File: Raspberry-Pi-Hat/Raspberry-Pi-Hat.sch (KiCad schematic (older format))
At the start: 60 parts, among them J1 Screw_Terminal_01x04, J2 Screw_Terminal_01x02, J3 40HAT, J4 Screw_Terminal_01x02, J5 USB_B, J6 CONN_02X02, J7 USB_A, J8 USB_A, J9 CONN_01X02, Q1 DMG2305UX, Q2 DMMT5401, U1 ADM3490ExR, U2 CAT24C32, U3 TCAN330, U4 LMZ13608

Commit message: changed footprint size
changed resistor and capacitor footprint size for 0603 when possible.
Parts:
- C10, C11, C12, C13, C16, C17, C18, C2, C3, C4, C5, C50, C51, C6, C7, C8, C9: footprint Capacitor_SMD:C_1206_3216Metric_Pad1.42x1.75mm_HandSolder -> Capacitor_SMD:C_0603_1608Metric_Pad1.05x0.95mm_HandSolder
- R1, R10, R2, R3, R4, R5: footprint Resistor_SMD:R_1206_3216Metric_Pad1.42x1.75mm_HandSolder -> Resistor_SMD:R_0603_1608Metric_Pad1.05x0.95mm_HandSolder
- R11, R23, R24, R6, R7, R8, R9: footprint Resistor_SMD:R_0603_1608Metric_Pad0.84x1.00mm_HandSolder -> Resistor_SMD:R_0603_1608Metric_Pad1.05x0.95mm_HandSolder
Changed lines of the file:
@@
 F 0 "R23" V 5830 3600 50  0000 C CNN
 F 1 "10K" V 5750 3600 50  0000 C CNN
-F 2 "Resistor_SMD:R_0603_1608Metric_Pad0.84x1.00mm_HandSolder" V 5680 3600 50  0001 C CNN
+F 2 "Resistor_SMD:R_0603_1608Metric_Pad1.05x0.95mm_HandSolder" V 5680 3600 50  0001 C CNN
 F 3 "" H 5750 3600 50  0001 C CNN
 	1    5750 3600
@@
 F 0 "R24" V 6630 3600 50  0000 C CNN
 F 1 "47K" V 6550 3600 50  0000 C CNN
-F 2 "Resistor_SMD:R_0603_1608Metric_Pad0.84x1.00mm_HandSolder" V 6480 3600 50  0001 C CNN
+F 2 "Resistor_SMD:R_0603_1608Metric_Pad1.05x0.95mm_HandSolder" V 6480 3600 50  0001 C CNN
 F 3 "" H 6550 3600 50  0001 C CNN
 	1    6550 3600
@@
 F 0 "R6" V 2430 7400 50  0000 C CNN
 F 1 "3.9K" V 2350 7400 50  0000 C CNN
-F 2 "Resistor_SMD:R_0603_1608Metric_Pad0.84x1.00mm_HandSolder" V 2280 7400 50  0001 C CNN
+F 2 "Resistor_SMD:R_0603_1608Metric_Pad1.05x0.95mm_HandSolder" V 2280 7400 50  0001 C CNN
 F 3 "" H 2350 7400 50  0001 C CNN
 	1    2350 7400
@@
 F 0 "R8" V 2430 7650 50  0000 C CNN
 F 1 "3.9K" V 2350 7650 50  0000 C CNN
-F 2 "Resistor_SMD:R_0603_1608Metric_Pad0.84x1.00mm_HandSolder" V 2280 7650 50  0001 C CNN
+F 2 "Resistor_SMD:R_0603_1608Metric_Pad1.05x0.95mm_HandSolder" V 2280 7650 50  0001 C CNN
 F 3 "" H 2350 7650 50  0001 C CNN
 	1    2350 7650
@@
 F 0 "R7" V 6180 4300 50  0000 C CNN
 F 1 "DNP" V 6100 4300 50  0000 C CNN
-F 2 "Resistor_SMD:R_0603_1608Metric_Pad0.84x1.00mm_HandSolder" V 6030 4300 50  0001 C CNN
+F 2 "Resistor_SMD:R_0603_1608Metric_Pad1.05x0.95mm_HandSolder" V 6030 4300 50  0001 C CNN
 F 3 "" H 6100 4300 50  0001 C CNN
 	1    6100 4300
@@
 F 0 "R9" V 6180 4950 50  0000 C CNN
 F 1 "DNP" V 6100 4950 50  0000 C CNN
-F 2 "Resistor_SMD:R_0603_1608Metric_Pad0.84x1.00mm_HandSolder" V 6030 4950 50  0001 C CNN
+F 2 "Resistor_SMD:R_0603_1608Metric_Pad1.05x0.95mm_HandSolder" V 6030 4950 50  0001 C CNN
 F 3 "" H 6100 4950 50  0001 C CNN
 	1    6100 4950
@@
 F 0 "R11" V 1380 6100 50  0000 C CNN
 F 1 "DNP" V 1300 6100 50  0000 C CNN
-F 2 "Resistor_SMD:R_0603_1608Metric_Pad0.84x1.00mm_HandSolder" V 1230 6100 50  0001 C CNN
+F 2 "Resistor_SMD:R_0603_1608Metric_Pad1.05x0.95mm_HandSolder" V 1230 6100 50  0001 C CNN
 F 3 "" H 1300 6100 50  0001 C CNN
 	1    1300 6100
@@
 F 0 "C10" H 12215 2046 50  0000 L CNN
 F 1 "470nF" H 12215 1955 50  0000 L CNN
-F 2 "Capacitor_SMD:C_1206_3216Metric_Pad1.42x1.75mm_HandSolder" H 12138 1850 50  0001 C CNN
+F 2 "Capacitor_SMD:C_0603_1608Metric_Pad1.05x0.95mm_HandSolder" H 12138 1850 50  0001 C CNN
 F 3 "~" H 12100 2000 50  0001 C CNN
 	1    12100 2000
@@
 F 0 "C16" H 15065 1796 50  0000 L CNN
 F 1 "47uF" H 15065 1705 50  0000 L CNN
-F 2 "Capacitor_SMD:C_1206_3216Metric_Pad1.42x1.75mm_HandSolder" H 14988 1600 50  0001 C CNN
+F 2 "Capacitor_SMD:C_0603_1608Metric_Pad1.05x0.95mm_HandSolder" H 14988 1600 50  0001 C CNN
 F 3 "~" H 14950 1750 50  0001 C CNN
 F 4 "X5R ceramic" H 14950 1750 50  0001 C CNN "Technologie"
@@
 F 0 "C17" H 15515 1796 50  0000 L CNN
 F 1 "47nF" H 15515 1705 50  0000 L CNN
-F 2 "Capacitor_SMD:C_1206_3216Metric_Pad1.42x1.75mm_HandSolder" H 15438 1600 50  0001 C CNN
+F 2 "Capacitor_SMD:C_0603_1608Metric_Pad1.05x0.95mm_HandSolder" H 15438 1600 50  0001 C CNN
 F 3 "~" H 15400 1750 50  0001 C CNN
 F 4 "X5R ceramic" H 15400 1750 50  0001 C CNN "Technologie"
@@
 F 0 "C18" H 15915 1796 50  0000 L CNN
 F 1 "47nF" H 15915 1705 50  0000 L CNN
-F 2 "Capacitor_SMD:C_1206_3216Metric_Pad1.42x1.75mm_HandSolder" H 15838 1600 50  0001 C CNN
+F 2 "Capacitor_SMD:C_0603_1608Metric_Pad1.05x0.95mm_HandSolder" H 15838 1600 50  0001 C CNN
 F 3 "~" H 15800 1750 50  0001 C CNN
 F 4 "X5R ceramic" H 15800 1750 50  0001 C CNN "Technologie"
@@
 F 0 "C9" H 11865 1796 50  0000 L CNN
 F 1 "47nF" H 11865 1705 50  0000 L CNN
-F 2 "Capacitor_SMD:C_1206_3216Metric_Pad1.42x1.75mm_HandSolder" H 11788 1600 50  0001 C CNN
+F 2 "Capacitor_SMD:C_0603_1608Metric_Pad1.05x0.95mm_HandSolder" H 11788 1600 50  0001 C CNN
 F 3 "~" H 11750 1750 50  0001 C CNN
 F 4 "X7R ceramic" H 11750 1750 50  0001 C CNN "Technologie"
@@
 F 0 "C6" H 11465 1796 50  0000 L CNN
 F 1 "47nF" H 11465 1705 50  0000 L CNN
-F 2 "Capacitor_SMD:C_1206_3216Metric_Pad1.42x1.75mm_HandSolder" H 11388 1600 50  0001 C CNN
+F 2 "Capacitor_SMD:C_0603_1608Metric_Pad1.05x0.95mm_HandSolder" H 11388 1600 50  0001 C CNN
 F 3 "~" H 11350 1750 50  0001 C CNN
 F 4 "X7R ceramic" H 11350 1750 50  0001 C CNN "Technologie"
@@
 F 0 "C4" H 11065 1796 50  0000 L CNN
 F 1 "10uF" H 11065 1705 50  0000 L CNN
-F 2 "Capacitor_SMD:C_1206_3216Metric_Pad1.42x1.75mm_HandSolder" H 10988 1600 50  0001 C CNN
+F 2 "Capacitor_SMD:C_0603_1608Metric_Pad1.05x0.95mm_HandSolder" H 10988 1600 50  0001 C CNN
 F 3 "~" H 10950 1750 50  0001 C CNN
 F 4 "X7R ceramic" H 10950 1750 50  0001 C CNN "Technologie"
@@
 F 0 "C3" H 10665 1796 50  0000 L CNN
 F 1 "10uF" H 10665 1705 50  0000 L CNN
-F 2 "Capacitor_SMD:C_1206_3216Metric_Pad1.42x1.75mm_HandSolder" H 10588 1600 50  0001 C CNN
+F 2 "Capacitor_SMD:C_0603_1608Metric_Pad1.05x0.95mm_HandSolder" H 10588 1600 50  0001 C CNN
 F 3 "~" H 10550 1750 50  0001 C CNN
 F 4 "X7R ceramic" H 10550 1750 50  0001 C CNN "Technologie"
@@
 F 0 "C2" H 10265 1796 50  0000 L CNN
 F 1 "10uF" H 10265 1705 50  0000 L CNN
-F 2 "Capacitor_SMD:C_1206_3216Metric_Pad1.42x1.75mm_HandSolder" H 10188 1600 50  0001 C CNN
+F 2 "Capacitor_SMD:C_0603_1608Metric_Pad1.05x0.95mm_HandSolder" H 10188 1600 50  0001 C CNN
 F 3 "~" H 10150 1750 50  0001 C CNN
 F 4 "X7R ceramic" H 10150 1750 50  0001 C CNN "Technologie"
@@
 F 0 "C8" H 11615 3646 50  0000 L CNN
 F 1 "100nF" H 11615 3555 50  0000 L CNN
-F 2 "Capacitor_SMD:C_1206_3216Metric_Pad1.42x1.75mm_HandSolder" H 11538 3450 50  0001 C CNN
+F 2 "Capacitor_SMD:C_0603_1608Metric_Pad1.05x0.95mm_HandSolder" H 11538 3450 50  0001 C CNN
 F 3 "~" H 11500 3600 50  0001 C CNN
 	1    11500 3600
@@
 F 0 "R5" H 12759 3896 50  0000 L CNN
 F 1 "R_Small" H 12759 3805 50  0000 L CNN
-F 2 "Resistor_SMD:R_1206_3216Metric_Pad1.42x1.75mm_HandSolder" H 12700 3850 50  0001 C CNN
+F 2 "Resistor_SMD:R_0603_1608Metric_Pad1.05x0.95mm_HandSolder" H 12700 3850 50  0001 C CNN
 F 3 "~" H 12700 3850 50  0001 C CNN
 	1    12700 3850
@@
 F 0 "R10" H 12759 4296 50  0000 L CNN
 F 1 "R_Small" H 12759 4205 50  0000 L CNN
-F 2 "Resistor_SMD:R_1206_3216Metric_Pad1.42x1.75mm_HandSolder" H 12700 4250 50  0001 C CNN
+F 2 "Resistor_SMD:R_0603_1608Metric_Pad1.05x0.95mm_HandSolder" H 12700 4250 50  0001 C CNN
 F 3 "~" H 12700 4250 50  0001 C CNN
 	1    12700 4250
@@
 F 0 "C13" V 13048 6200 50  0000 C CNN
 F 1 "C" V 13139 6200 50  0000 C CNN
-F 2 "Capacitor_SMD:C_1206_3216Metric_Pad1.42x1.75mm_HandSolder" H 13338 6050 50  0001 C CNN
+F 2 "Capacitor_SMD:C_0603_1608Metric_Pad1.05x0.95mm_HandSolder" H 13338 6050 50  0001 C CNN
 F 3 "~" H 13300 6200 50  0001 C CNN
 	1    13300 6200
@@
 F 0 "C12" H 13035 6754 50  0000 R CNN
 F 1 "C" H 13035 6845 50  0000 R CNN
-F 2 "Capacitor_SMD:C_1206_3216Metric_Pad1.42x1.75mm_HandSolder" H 13188 6650 50  0001 C CNN
+F 2 "Capacitor_SMD:C_0603_1608Metric_Pad1.05x0.95mm_HandSolder" H 13188 6650 50  0001 C CNN
 F 3 "~" H 13150 6800 50  0001 C CNN
 	1    13150 6800
@@
 F 0 "C11" H 13035 5554 50  0000 R CNN
 F 1 "C" H 13035 5645 50  0000 R CNN
-F 2 "Capacitor_SMD:C_1206_3216Metric_Pad1.42x1.75mm_HandSolder" H 13188 5450 50  0001 C CNN
+F 2 "Capacitor_SMD:C_0603_1608Metric_Pad1.05x0.95mm_HandSolder" H 13188 5450 50  0001 C CNN
 F 3 "~" H 13150 5600 50  0001 C CNN
 	1    13150 5600
@@
 F 0 "C7" H 11285 6404 50  0000 R CNN
 F 1 "100nF" H 11285 6495 50  0000 R CNN
-F 2 "Capacitor_SMD:C_1206_3216Metric_Pad1.42x1.75mm_HandSolder" H 11438 6300 50  0001 C CNN
+F 2 "Capacitor_SMD:C_0603_1608Metric_Pad1.05x0.95mm_HandSolder" H 11438 6300 50  0001 C CNN
 F 3 "~" H 11400 6450 50  0001 C CNN
 	1    11400 6450
@@
 F 0 "R1" V 10554 6050 50  0000 C CNN
 F 1 "R" V 10645 6050 50  0000 C CNN
-F 2 "Resistor_SMD:R_1206_3216Metric_Pad1.42x1.75mm_HandSolder" H 10750 6050 50  0001 C CNN
+F 2 "Resistor_SMD:R_0603_1608Metric_Pad1.05x0.95mm_HandSolder" H 10750 6050 50  0001 C CNN
 F 3 "~" H 10750 6050 50  0001 C CNN
 	1    10750 6050
@@
 F 0 "R2" V 10554 6150 50  0000 C CNN
 F 1 "R" V 10645 6150 50  0000 C CNN
-F 2 "Resistor_SMD:R_1206_3216Metric_Pad1.42x1.75mm_HandSolder" H 10750 6150 50  0001 C CNN
+F 2 "Resistor_SMD:R_0603_1608Metric_Pad1.05x0.95mm_HandSolder" H 10750 6150 50  0001 C CNN
 F 3 "~" H 10750 6150 50  0001 C CNN
 	1    10750 6150
@@
 F 0 "C5" H 11085 6404 50  0000 R CNN
 F 1 "C" H 11085 6495 50  0000 R CNN
-F 2 "Capacitor_SMD:C_1206_3216Metric_Pad1.42x1.75mm_HandSolder" H 11238 6300 50  0001 C CNN
+F 2 "Capacitor_SMD:C_0603_1608Metric_Pad1.05x0.95mm_HandSolder" H 11238 6300 50  0001 C CNN
 F 3 "~" H 11200 6450 50  0001 C CNN
 	1    11200 6450
@@
 F 0 "R4" V 11004 4250 50  0000 C CNN
 F 1 "R" V 11095 4250 50  0000 C CNN
-F 2 "Resistor_SMD:R_1206_3216Metric_Pad1.42x1.75mm_HandSolder" H 11200 4250 50  0001 C CNN
+F 2 "Resistor_SMD:R_0603_1608Metric_Pad1.05x0.95mm_HandSolder" H 11200 4250 50  0001 C CNN
 F 3 "~" H 11200 4250 50  0001 C CNN
 	1    11200 4250
@@
 F 0 "R3" V 11004 3850 50  0000 C CNN
 F 1 "R" V 11095 3850 50  0000 C CNN
-F 2 "Resistor_SMD:R_1206_3216Metric_Pad1.42x1.75mm_HandSolder" H 11200 3850 50  0001 C CNN
+F 2 "Resistor_SMD:R_0603_1608Metric_Pad1.05x0.95mm_HandSolder" H 11200 3850 50  0001 C CNN
 F 3 "~" H 11200 3850 50  0001 C CNN
 	1    11200 3850
@@
 F 0 "C51" H 13685 8204 50  0000 R CNN
 F 1 "100nF" H 13685 8295 50  0000 R CNN
-F 2 "Capacitor_SMD:C_1206_3216Metric_Pad1.42x1.75mm_HandSolder" H 13838 8100 50  0001 C CNN
+F 2 "Capacitor_SMD:C_0603_1608Metric_Pad1.05x0.95mm_HandSolder" H 13838 8100 50  0001 C CNN
 F 3 "~" H 13800 8250 50  0001 C CNN
 	1    13800 8250
@@
 F 0 "C50" H 13285 9004 50  0000 R CNN
 F 1 "100nF" H 13285 9095 50  0000 R CNN
-F 2 "Capacitor_SMD:C_1206_3216Metric_Pad1.42x1.75mm_HandSolder" H 13438 8900 50  0001 C CNN
+F 2 "Capacitor_SMD:C_0603_1608Metric_Pad1.05x0.95mm_HandSolder" H 13438 8900 50  0001 C CNN
 F 3 "~" H 13400 9050 50  0001 C CNN
 	1    13400 9050

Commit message: Routted diff pair
All USB lines is routed and most of the signal lines is routed as well.
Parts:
- removed J6: CONN_02X02, Connector_PinHeader_2.54mm:PinHeader_2x02_P2.54mm_Vertical, symbol Connector_Generic:Conn_02x02_Odd_Even
- removed R7, R9: DNP, Resistor_SMD:R_0603_1608Metric_Pad1.05x0.95mm_HandSolder, symbol Device:R
- added C54, C55: 1uF, Capacitor_SMD:C_0603_1608Metric_Pad1.05x0.95mm_HandSolder, symbol Device:C
- added J10, J6: Conn_01x03, Connector_PinHeader_2.54mm:PinHeader_1x03_P2.54mm_Vertical, symbol Connector_Generic:Conn_01x03
- added U11: TLV71211_SOT23-5, Package_TO_SOT_SMD:SOT-23-5, symbol Regulator_Linear:TLV71211_SOT23-5
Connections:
- net P3V3_HAT is gone; now on net +3V3: J3.1 (P3V3)
- net +5V: now also Q1.2 (S), Q2.5 (E), C54.1, U11.1 (IN), U11.3 (EN); no longer Q1.3 (D), Q2.6 (E)
- net GND: now also C54.2, C55.2, U11.2 (GND)
- net RXD(GPIO15): now also J10.2 (Pin_2)
- net RX_CAN: now also J6.3 (Pin_3)
- net RX_NMEA183: now also J6.1 (Pin_1)
- net TXD(GPIO14): now also J6.2 (Pin_2)
- net TX_CAN: now also J10.3 (Pin_3)
- net TX_NMEA183: now also J10.1 (Pin_1)
- net P5V_HAT renamed P5V
- net P5V: now also Q1.3 (D), Q2.6 (E); no longer Q1.2 (S), Q2.5 (E)
- new net +1V1: C55.1, U11.5 (OUT)
- no-connect marks 23 -> 28

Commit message: Change strategy
Remove USB hub, connect CAN to SPI and NMEA to RSPI serial.
Addition of RTC
Addition of Fan PWM connector
Plan to add a soft start button
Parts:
- removed C50, C51: 100nF, Capacitor_SMD:C_0603_1608Metric_Pad1.05x0.95mm_HandSolder, symbol Device:C
- removed C54, C55: 1uF, Capacitor_SMD:C_0603_1608Metric_Pad1.05x0.95mm_HandSolder, symbol Device:C
- removed FB3, FB4: 200 @ 100MHz, Resistor_SMD:R_0805_2012Metric_Pad1.15x1.40mm_HandSolder, symbol Device:Ferrite_Bead_Small
- removed J10, J6: Conn_01x03, Connector_PinHeader_2.54mm:PinHeader_1x03_P2.54mm_Vertical, symbol Connector_Generic:Conn_01x03
- removed J5: USB_B, Connector_USB:USB_B_Lumberg_2411_02_Horizontal, symbol Connector:USB_B
- removed J7, J8: USB_A, Connector_USB:USB_A_Molex_67643_Horizontal, symbol Connector:USB_A
- removed U11: TLV71211_SOT23-5, Package_TO_SOT_SMD:SOT-23-5, symbol Regulator_Linear:TLV71211_SOT23-5
- added BT1: Battery_Cell, symbol Device:Battery_Cell
- added C19: 47pF, Capacitor_SMD:C_0603_1608Metric_Pad1.05x0.95mm_HandSolder, symbol Device:C
- added C20, C25: 100nF, Capacitor_SMD:C_0603_1608Metric_Pad1.05x0.95mm_HandSolder, symbol Device:C
- added C21, C22: nc, Capacitor_SMD:C_0603_1608Metric_Pad1.05x0.95mm_HandSolder, symbol Device:C
- added C23, C24: 30pF, Capacitor_SMD:C_0603_1608Metric_Pad1.05x0.95mm_HandSolder, symbol Device:C
- added J5: Conn_01x04, Connector_PinHeader_2.54mm:PinHeader_1x04_P2.54mm_Horizontal, symbol Connector_Generic:Conn_01x04
- added R16, R17, R18, R19: 10k, Resistor_SMD:R_0603_1608Metric_Pad1.05x0.95mm_HandSolder, symbol Device:R_Small
- added R7: TBD, Resistor_SMD:R_0603_1608Metric_Pad1.05x0.95mm_HandSolder, symbol Device:R_Small
- added R9: NC, Resistor_SMD:R_0603_1608Metric_Pad1.05x0.95mm_HandSolder, symbol Device:R_Small
- added U5: AB0805, Package_DFN_QFN:VQFN-16-1EP_3x3mm_P0.5mm_EP1.8x1.8mm, symbol Timer_RTC:AB0805
- added U6: MCP2515-xSO, Package_SO:SOIC-18W_7.5x11.6mm_P1.27mm, symbol Interface_CAN_LIN:MCP2515-xSO
- added Y1: 32.768 kHz, Crystal:Crystal_C26-LF_D2.1mm_L6.5mm_Horizontal, symbol Device:Crystal
- added Y2: 8MHz, Crystal:Crystal_SMD_Abracon_ABM3-2Pin_5.0x3.2mm_HandSoldering, symbol Device:Crystal
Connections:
- net RXD(GPIO15) is gone; now on net TX_NMEA183: J3.10 (BCM15)
- net TXD(GPIO14) is gone; now on net RX_NMEA183: J3.8 (BCM14)
- net +3V3: now also C20.2, C25.2, R16.2, R17.2, R18.2, R19.2, R9.2, U5.13 (VCC), U6.18 (VDD)
- net GND: now also BT1.2 (-), C19.2, C20.1, C21.1, C22.1, C23.2, C24.2, C25.1, U5.10 (EXTI), U5.17 (VSS), U5.2 (WDI), U5.9 (VSS), U6.9 (VSS)
- net I2C-SCL-(GPIO3): now also U5.7 (SCL)
- net I2C-SDA-(GPIO2): now also U5.6 (SDA)
- net RX_CAN: now also U6.1 (TXCAN)
- net SPI-CLK-(GPIO11): now also R9.1, U6.13 (SCK)
- net SPI-MISO-(GPIO9): now also R17.1, U6.15 (SO)
- net SPI-MOSI-(GPIO10): now also R18.1, U6.14 (SI)
- net TX_CAN: now also U6.2 (RXCAN)
- net FAN-RPM-(GPIO24): now reaches J3.18 (BCM24)
- net SPI-CS-(GPIO8): now reaches J3.24 (BCM8)
- net SPI-CS-(GPIO8): now also R16.1, U6.16 (~CS)
- net FAN-PWM-(GPIO12): now reaches J3.32 (BCM12)
- new net: R19.1, U6.17 (~RESET)
- new net: C23.1, U6.7 (OSC2), Y2.1
- new net: C24.1, U6.8 (OSC1), Y2.2
- new net: C19.1, U5.14 (AF)
- new net: C22.2, U5.15 (XO), Y1.2
- new net: C21.2, U5.16 (XI), Y1.1
- new net: R7.2, U5.5 (VBAT)
- new net: BT1.1 (+), R7.1
- no-connect marks 28 -> 30

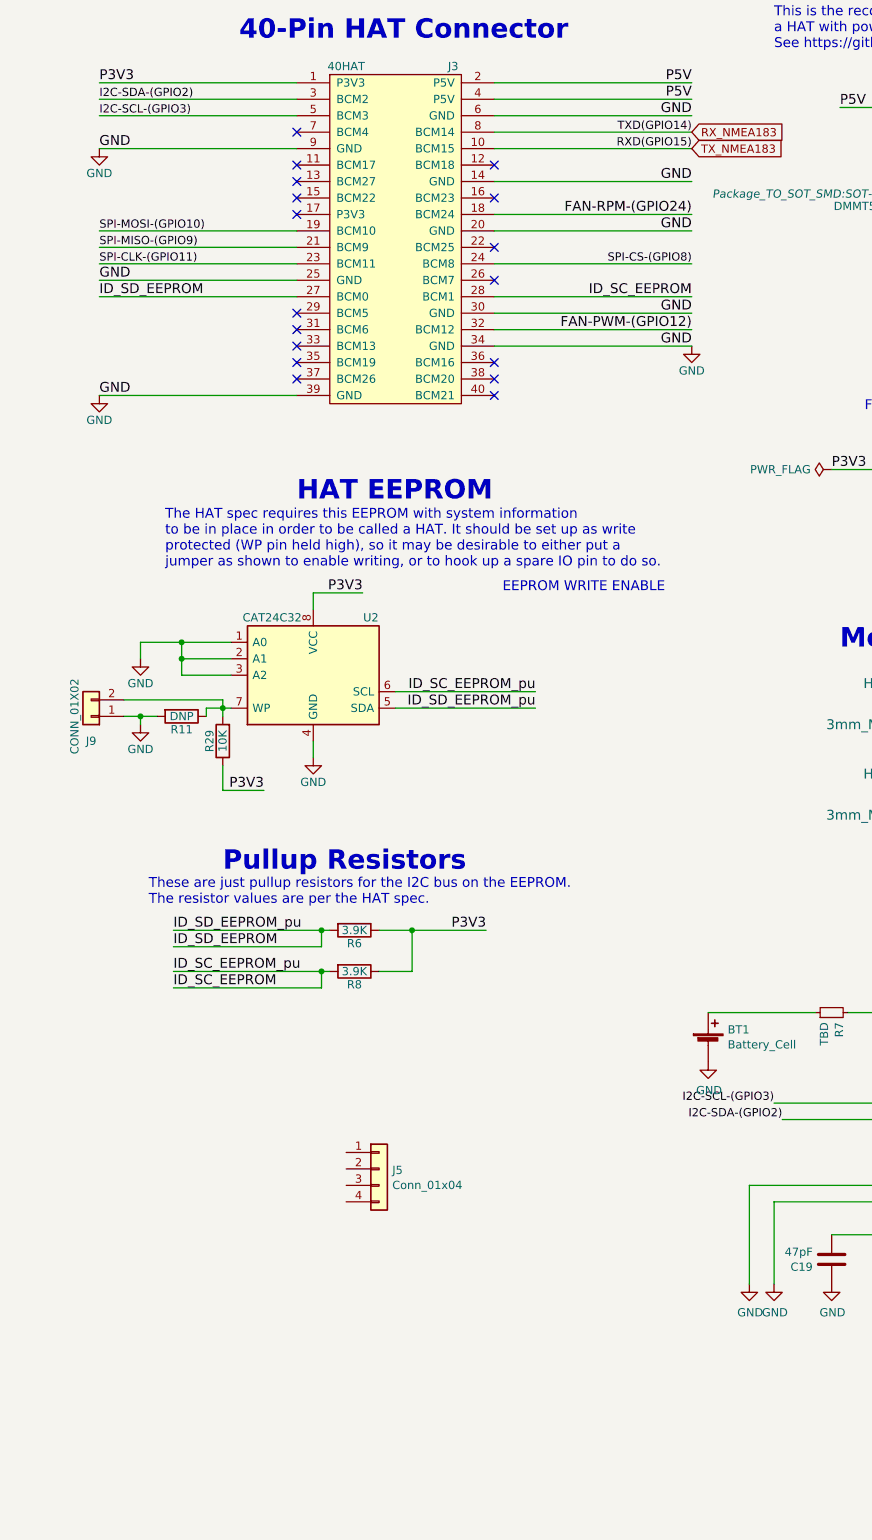
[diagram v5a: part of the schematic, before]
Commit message: Routing version SPI V0
Replaced USB with SPI for N2K
Power button
RTC

Routing done
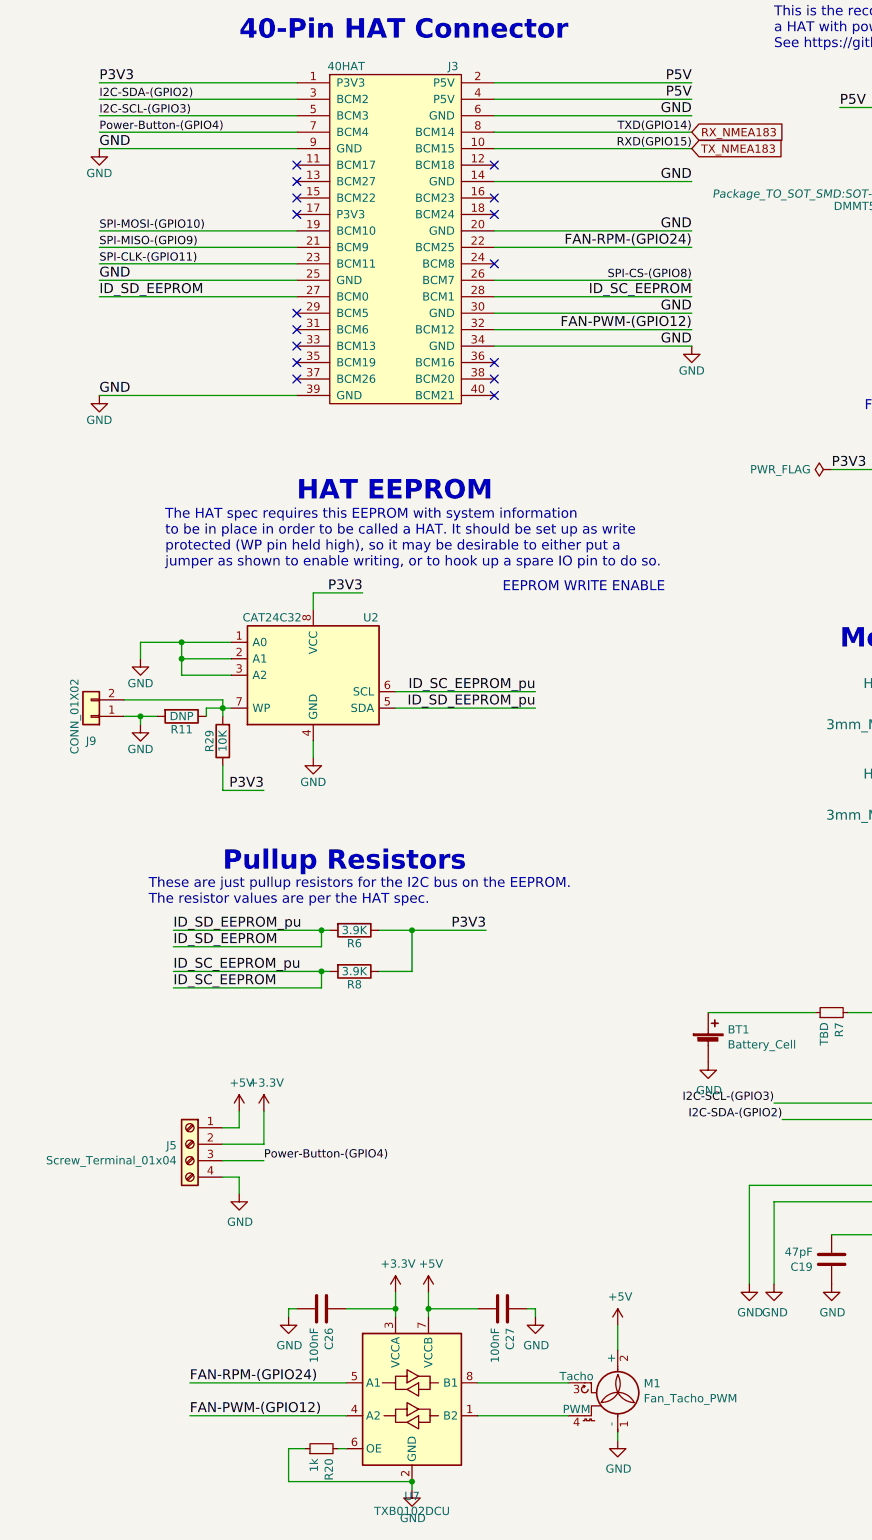
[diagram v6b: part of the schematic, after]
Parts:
- removed J5: Conn_01x04, Connector_PinHeader_2.54mm:PinHeader_1x04_P2.54mm_Horizontal, symbol Connector_Generic:Conn_01x04
- added C26, C27: 100nF, Capacitor_SMD:C_0805_2012Metric_Pad1.15x1.40mm_HandSolder, symbol Device:C
- added J5: Screw_Terminal_01x04, Connector_Phoenix_MSTB:PhoenixContact_MSTBVA_2,5_4-G-5,08_1x04_P5.08mm_Vertical, symbol Connector:Screw_Terminal_01x04
- added M1: Fan_Tacho_PWM, Connector:FanPinHeader_1x04_P2.54mm_Vertical, symbol Motor:Fan_Tacho_PWM
- added R20: 1k, Resistor_SMD:R_0805_2012Metric_Pad1.15x1.40mm_HandSolder, symbol Device:R_Small
- added U7: TXB0102DCU, Package_SO:VSSOP-8_2.4x2.1mm_P0.5mm, symbol Logic_LevelTranslator:TXB0102DCU
- BT1: footprint (none) -> Battery:BatteryHolder_Keystone_2998_1x6.8mm
- C10, C11, C12, C13, C16, C17, C18, C19, C2, C20, C21, C22, C23, C24, C25, C3, C4, C5, C6, C7, C8, C9: footprint Capacitor_SMD:C_0603_1608Metric_Pad1.05x0.95mm_HandSolder -> Capacitor_SMD:C_0805_2012Metric_Pad1.15x1.40mm_HandSolder
- R1, R10, R11, R12, R13, R14, R15, R16, R17, R18, R19, R2, R23, R24, R29, R3, R4, R5, R6, R7, R8, R9: footprint Resistor_SMD:R_0603_1608Metric_Pad1.05x0.95mm_HandSolder -> Resistor_SMD:R_0805_2012Metric_Pad1.15x1.40mm_HandSolder
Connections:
- net +3V3: now also C26.2, J5.2 (Pin_2), U7.3 (VCCA)
- net +5V: now also C27.1, J5.1 (Pin_1), M1.2 (+), U7.7 (VCCB)
- net FAN-PWM-(GPIO12): now also U7.4 (A2)
- net FAN-RPM-(GPIO24): now also J3.22 (BCM25), U7.5 (A1); no longer J3.18 (BCM24)
- net GND: now also C26.1, C27.2, J5.4 (Pin_4), M1.1 (-), R20.1, U7.2 (GND)
- net SPI-CS-(GPIO8): now also J3.26 (BCM7); no longer J3.24 (BCM8)
- net Power-Button-(GPIO4): now reaches J3.7 (BCM4)
- net Power-Button-(GPIO4): now also J5.3 (Pin_3)
- new net: M1.3 (Tacho), U7.8 (B1)
- new net: M1.4 (PWM), U7.1 (B2)
- new net: R20.2, U7.6 (OE)
- no-connect marks 30 -> 29
